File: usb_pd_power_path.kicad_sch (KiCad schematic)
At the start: 80 parts

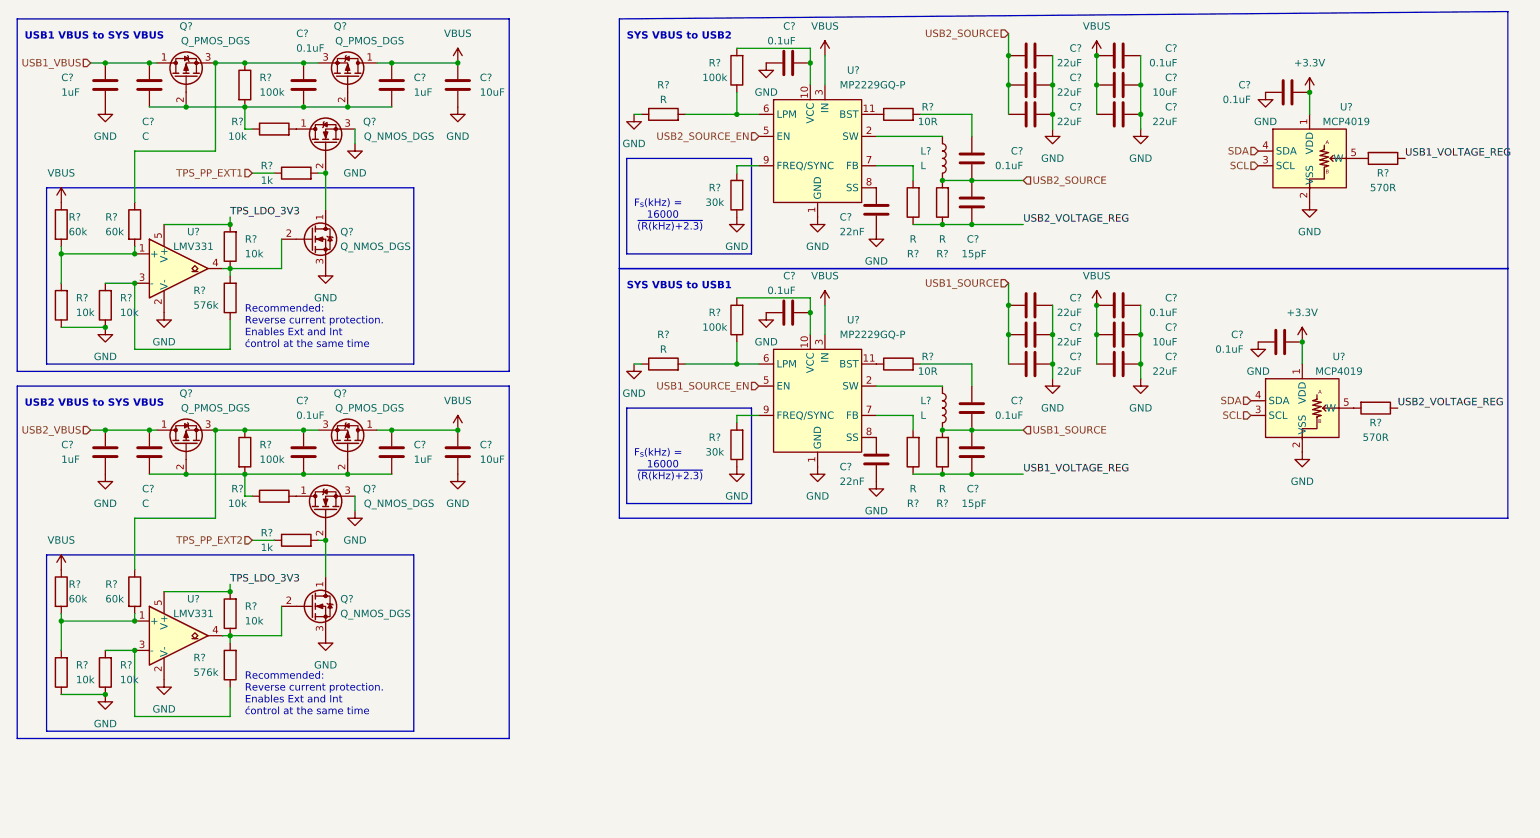
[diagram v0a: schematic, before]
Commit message: added audio ref schematic, added bat to 5V, added shift register, connected devices with other periferals
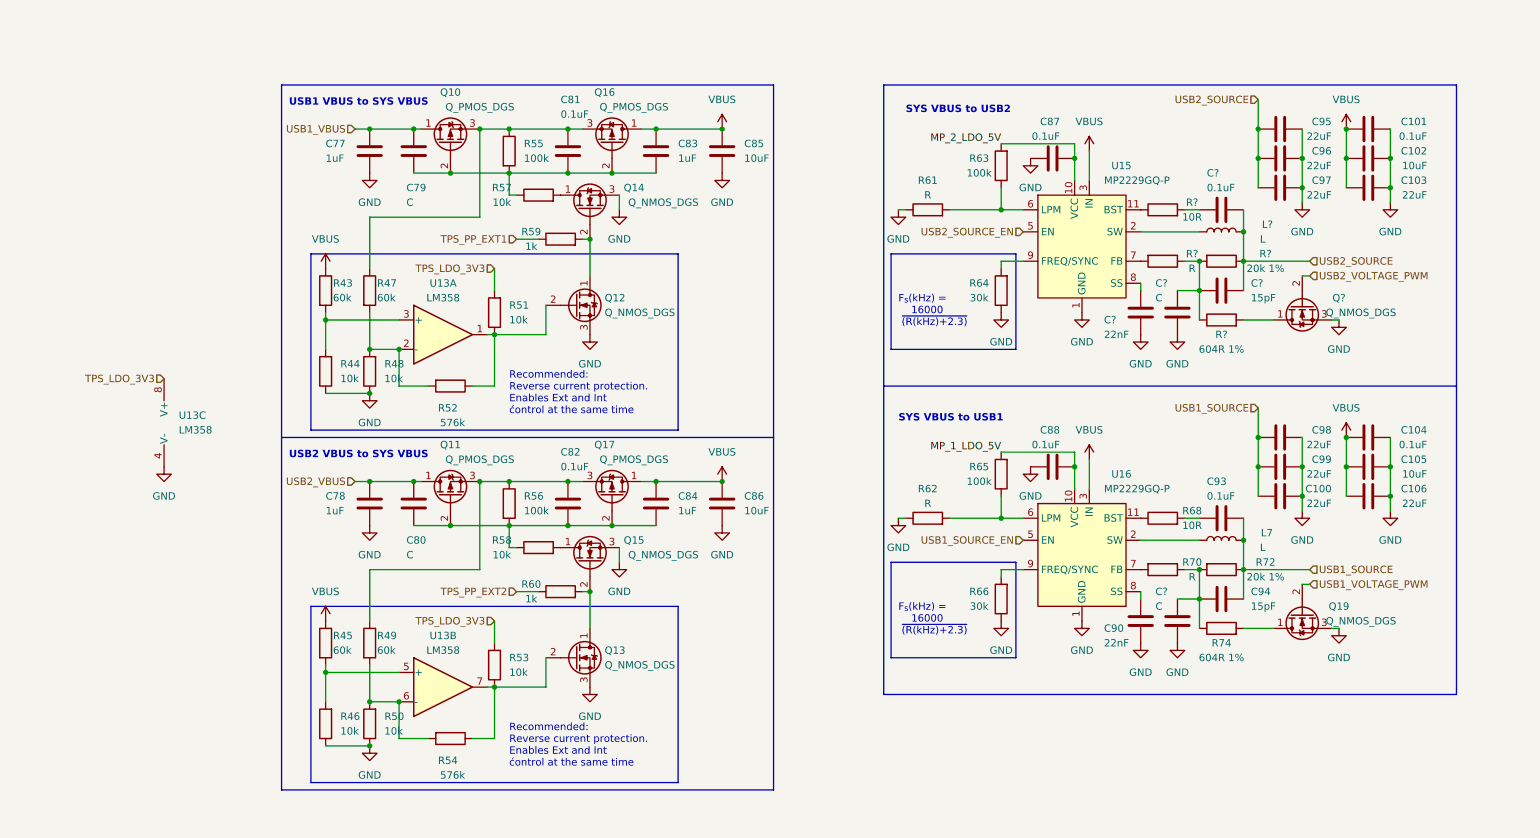
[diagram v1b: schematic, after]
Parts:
- removed C?: 22nF, symbol Device:C
- removed C? (x3): 0.1uF, symbol Device:C
- removed C?: 15pF, symbol Device:C
- removed L?: L, symbol Device:L
- removed R? (x2): 570R, symbol Device:R
- removed R? (x2): R, symbol Device:R
- removed R?: 10R, symbol Device:R
- removed U? (x2): MCP4019, Package_TO_SOT_SMD:SOT-353_SC-70-5_Handsoldering, symbol airsoft_controller:MCP4019
- removed U? (x2): LMV331, symbol Comparator:LMV331
- added C?: 15pF, symbol Device:C
- added C?: 0.1uF, symbol Device:C
- added C?: 22nF, symbol Device:C
- added C? (x2): C, symbol Device:C
- added L?: L, symbol Device:L
- added Q19, Q?: Q_NMOS_DGS, symbol Device:Q_NMOS_DGS
- added R74, R?: 604R 1%, symbol Device:R
- added R?: 10R, symbol Device:R
- added R?: 20k 1%, symbol Device:R
- added R?: R, symbol Device:R
- added U13: LM358, symbol Amplifier_Operational:LM358
- R72: renamed from R?; value R -> 20k 1%
- gave numbers to parts that had none: 64
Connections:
- net GND: now also C?.2, C?.2, C?.2, Q19.3 (S), Q?.3 (S), U13.4 (V-)
- net TPS_LDO_3V3: now also U13.8 (V+)
- net USB1_SOURCE: now also C94.1, R72.1; no longer C94.2, R72.2
- net USB2_SOURCE: now also C?.1, C?.1, L?.2, R?.1
- net at R48.2: now also R47.2, R52.2, U13.2 (-); no longer R52.1
- net at U15.8 (SS): now also C?.1
- net MP_2_LDO_5V: now reaches C87.2, R63.2, U15.10 (VCC)
- net at Q12.2 (G), R51.1: now also R52.1, U13.1; no longer R52.2
- net at R43.2, R44.2: now also U13.3 (+); no longer R47.2
- net at R45.2, R46.2: now also U13.5 (+); no longer R49.2
- net at R50.2: now also R49.2, R54.2, U13.6 (-); no longer R54.1
- net at Q13.2 (G), R53.1: now also R54.1, U13.7; no longer R54.2
- net at U15.2 (SW), U15.4 (SW): now also L?.1
- net MP_1_LDO_5V: now reaches C88.2, R65.2, U16.10 (VCC)
- net at U15.7 (FB): now also R?.2
- net at U15.11 (BST): now also R?.1
- removed net USB1_VOLTAGE_REG: C94.1, R70.1, R72.1
- new net: Q?.1 (D), R?.2
- new net: C94.2, C?.1, R70.1, R72.2, R74.1
- new net: Q19.1 (D), R74.2
- new net: C?.1, C?.2, R?.1, R?.1, R?.2
- new net: C?.2, R?.2
- new net USB1_VOLTAGE_PWM: Q19.2 (G)
- new net USB2_VOLTAGE_PWM: Q?.2 (G)
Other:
- moved on the sheet: C100, C101, C102, C103, C104, C105, C106, C77, C78, C79, C80, C81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

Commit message: added adcin2 config description, fixed some rule check errors
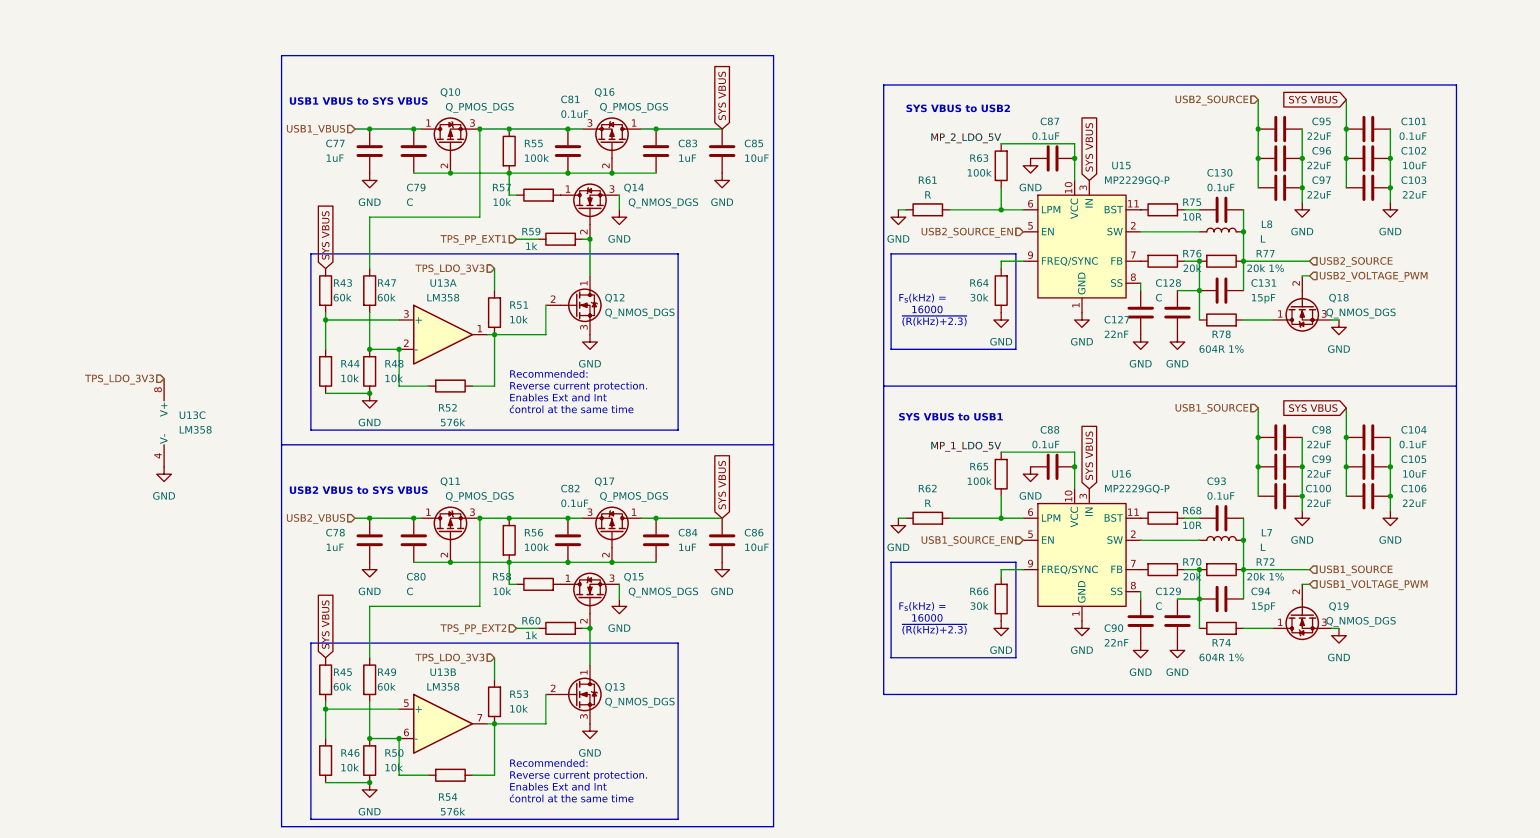
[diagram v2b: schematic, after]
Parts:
- R70: value R -> 20k
- R76: renamed from R?; value R -> 20k
- gave numbers to parts that had none: 10
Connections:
- net VBUS renamed SYS VBUS
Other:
- moved on the sheet: C78, C80, C82, C84, C86, Q11, Q13, Q15, Q17, R45, R46, R49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

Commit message: minor optimized pinassignement, added capacitors, added connectors
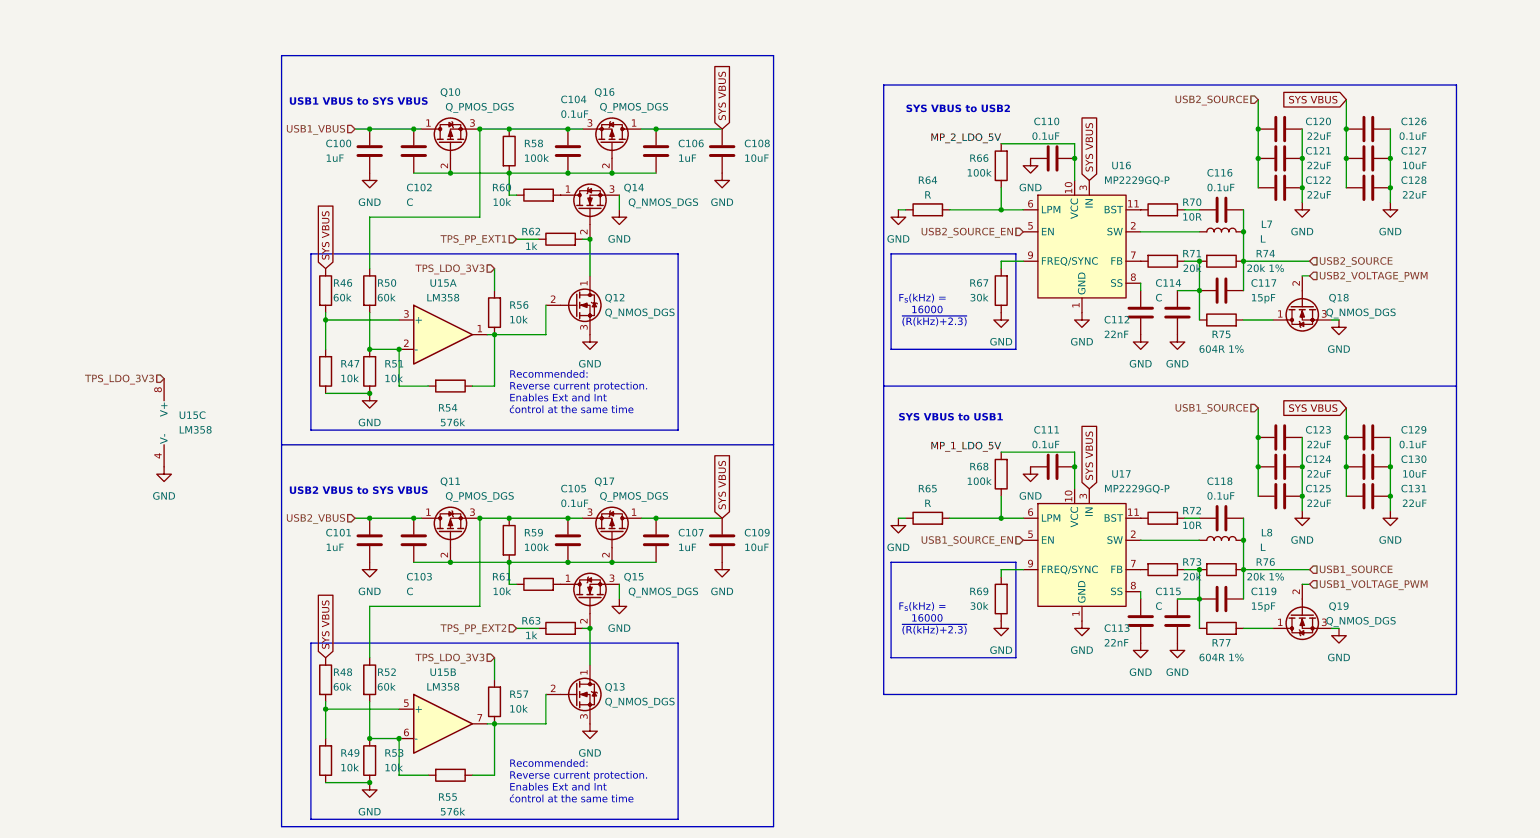
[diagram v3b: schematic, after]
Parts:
- renumbered C77 to C100, C78 to C101, C79 to C102, C80 to C103, C81 to C104, C82 to C105, C83 to C106, C84 to C107, C85 to C108, C86 to C109, C87 to C110, C88 to C111, C127 to C112, C90 to C113, C128 to C114, C129 to C115, C130 to C116, C131 to C117, C93 to C118, C94 to C119, C95 to C120, C96 to C121, C97 to C122, C98 to C123, C99 to C124, C100 to C125, C101 to C126, C102 to C127, C103 to C128, C104 to C129, C105 to C130, C106 to C131, L8 to L7, L7 to L8, R43 to R46, R44 to R47, R45 to R48, R46 to R49, R47 to R50, R48 to R51, R49 to R52, R50 to R53, R52 to R54, R54 to R55, R51 to R56, R53 to R57, R55 to R58, R56 to R59, R57 to R60, R58 to R61, R59 to R62, R60 to R63, R61 to R64, R62 to R65, R63 to R66, R64 to R67, R65 to R68, R66 to R69, R75 to R70, R76 to R71, R68 to R72, R70 to R73, R77 to R74, R78 to R75, R72 to R76, R74 to R77, U13 to U15, U15 to U16, U16 to U17

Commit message: PI LC lowpass filter, added CP2012 reset, added connectors
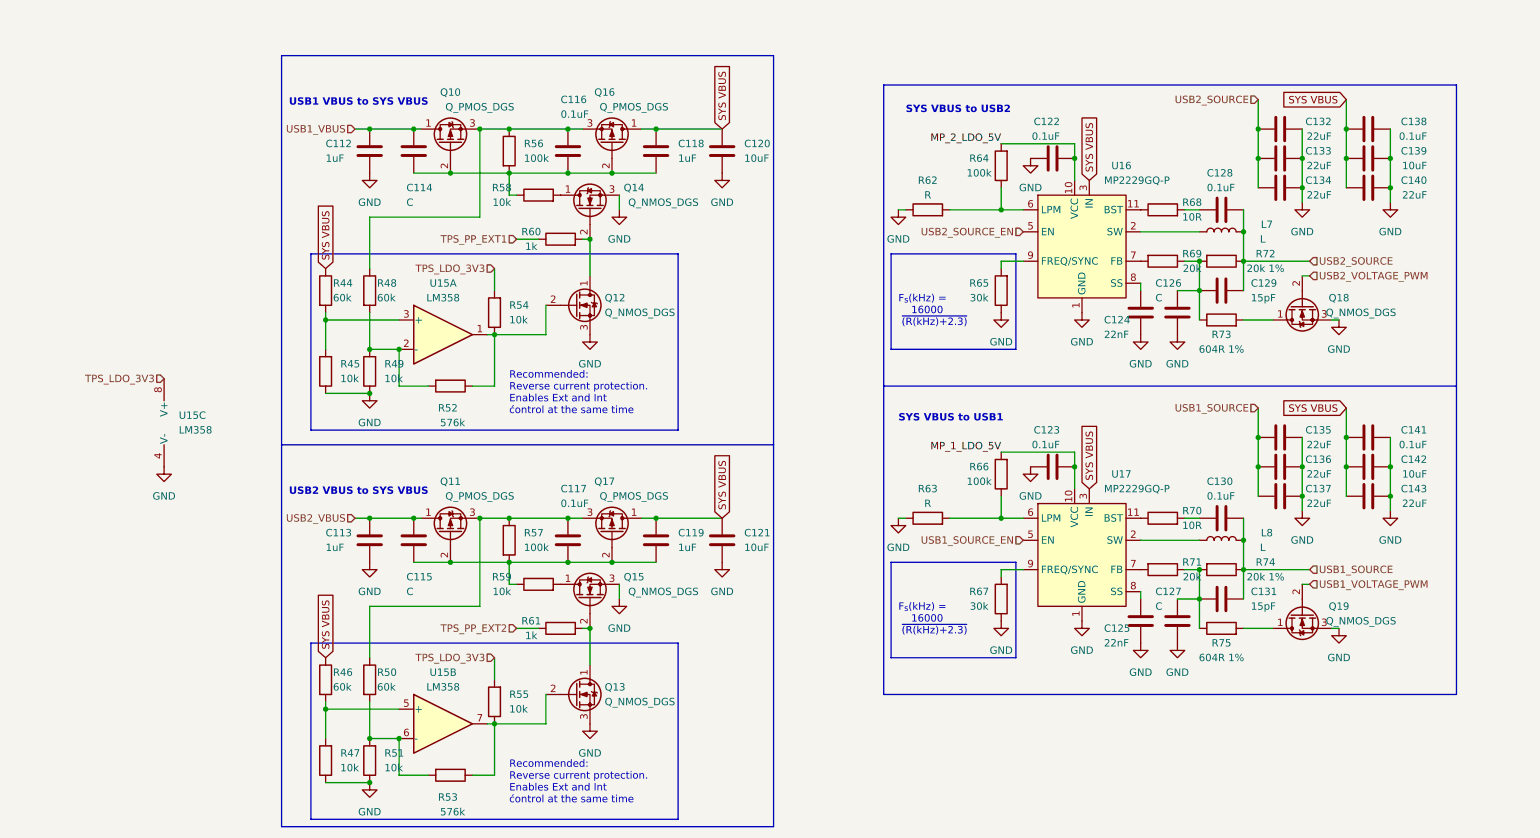
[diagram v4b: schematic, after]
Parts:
- renumbered C100 to C112, C101 to C113, C102 to C114, C103 to C115, C104 to C116, C105 to C117, C106 to C118, C107 to C119, C108 to C120, C109 to C121, C110 to C122, C111 to C123, C112 to C124, C113 to C125, C114 to C126, C115 to C127, C116 to C128, C117 to C129, C118 to C130, C119 to C131, C120 to C132, C121 to C133, C122 to C134, C123 to C135, C124 to C136, C125 to C137, C126 to C138, C127 to C139, C128 to C140, C129 to C141, C130 to C142, C131 to C143, R46 to R44, R47 to R45, R48 to R46, R49 to R47, R50 to R48, R51 to R49, R52 to R50, R53 to R51, R54 to R52, R55 to R53, R56 to R54, R57 to R55, R58 to R56, R59 to R57, R60 to R58, R61 to R59, R62 to R60, R63 to R61, R64 to R62, R65 to R63, R66 to R64, R67 to R65, R68 to R66, R69 to R67, R70 to R68, R71 to R69, R72 to R70, R73 to R71, R74 to R72, R75 to R73, R76 to R74, R77 to R75

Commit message: datasheet checkout, added couple of capacitors for usb-c, groupd some scheatics
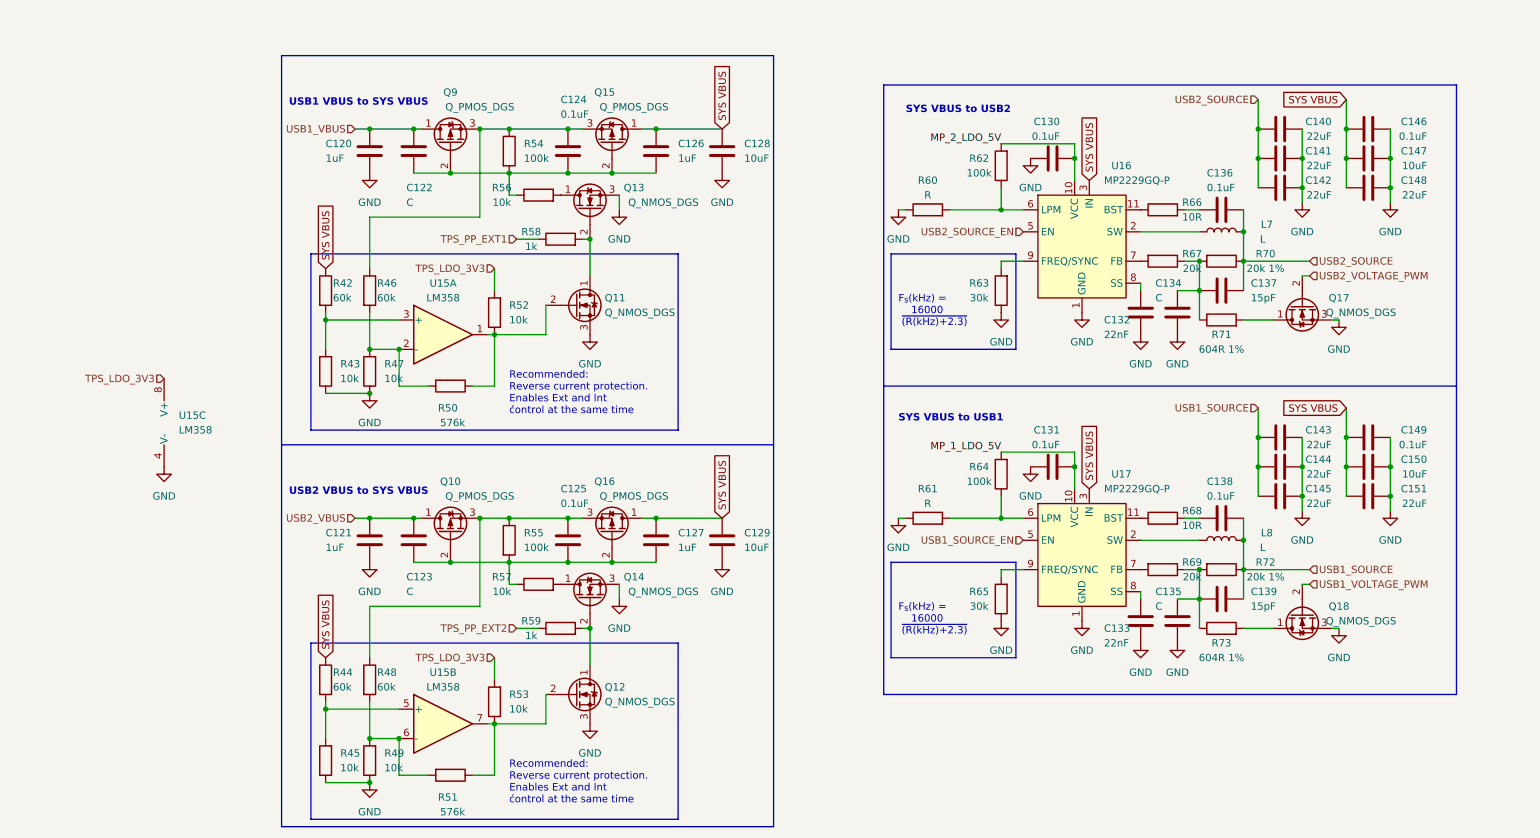
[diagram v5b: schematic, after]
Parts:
- renumbered C112 to C120, C113 to C121, C114 to C122, C115 to C123, C116 to C124, C117 to C125, C118 to C126, C119 to C127, C120 to C128, C121 to C129, C122 to C130, C123 to C131, C124 to C132, C125 to C133, C126 to C134, C127 to C135, C128 to C136, C129 to C137, C130 to C138, C131 to C139, C132 to C140, C133 to C141, C134 to C142, C135 to C143, C136 to C144, C137 to C145, C138 to C146, C139 to C147, C140 to C148, C141 to C149, C142 to C150, C143 to C151, Q11 to Q10, Q12 to Q11, Q13 to Q12, Q14 to Q13, Q15 to Q14, Q16 to Q15, Q17 to Q16, Q18 to Q17, Q19 to Q18, Q10 to Q9, R44 to R42, R45 to R43, R46 to R44, R47 to R45, R48 to R46, R49 to R47, R50 to R48, R51 to R49, R52 to R50, R53 to R51, R54 to R52, R55 to R53, R56 to R54, R57 to R55, R58 to R56, R59 to R57, R60 to R58, R61 to R59, R62 to R60, R63 to R61, R64 to R62, R65 to R63, R66 to R64, R67 to R65, R68 to R66, R69 to R67, R70 to R68, R71 to R69, R72 to R70, R73 to R71, R74 to R72, R75 to R73
